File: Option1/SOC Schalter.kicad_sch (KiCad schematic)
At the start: 2 parts, among them Q1101 AON6284

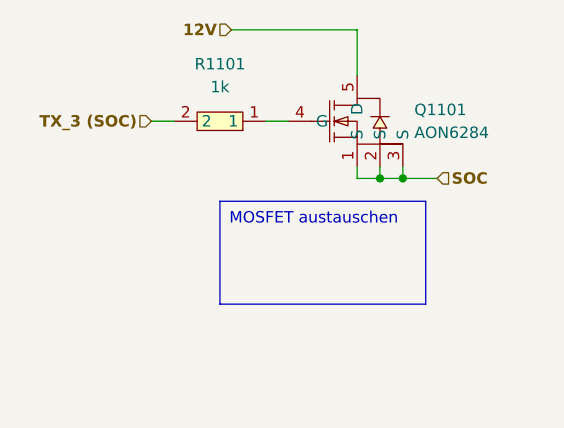
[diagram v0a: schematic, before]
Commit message: SPI Flash hinzugefügt, IN/Outputs vereinheitlicht, USB Flash Möglichkeit hinzugefügt, Display fehtl noch
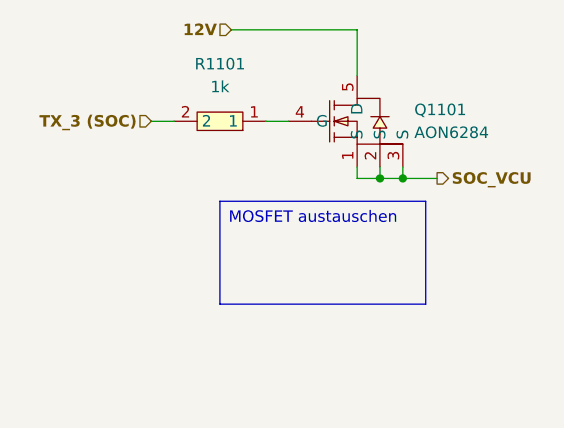
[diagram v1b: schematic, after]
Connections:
- net SOC renamed SOC_VCU
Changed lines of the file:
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@@
 (kicad_sch
-	(version 20231120)
+	(version 20250114)
 	(generator "eeschema")
-	(generator_version "8.0")
+	(generator_version "9.0")
 	(paper "A4")
 	(title_block
@@
 		(comment 2 "Bachelorarbiet")
 		(comment 3 "Sebastian Hampl")
+	)
+	(text_box "MOSFET austauschen"
+		(exclude_from_sim no)
+		(at 123.19 91.44 0)
+		(size 22.86 11.43)
+		(margins 0.9525 0.9525 0.9525 0.9525)
+		(stroke
+			(width 0)
+			(type default)
+			(color 255 0 0 1)
+		)
+		(fill
+			(type none)
+		)
+		(effects
+			(font
+				(size 1.27 1.27)
+			)
+			(justify left top)
+		)
 	)
 	(junction
@@
 		)
 	)
-	(text_box "MOSFET austauschen"
-		(exclude_from_sim no)
-		(at 123.19 91.44 0)
-		(size 22.86 11.43)
-		(stroke
-			(width 0)
-			(type default)
-			(color 255 0 0 1)
-		)
-		(fill
-			(type none)
-		)
-		(effects
-			(font
-				(size 1.27 1.27)
-			)
-			(justify left top)
-		)
-	)
-	(hierarchical_label "SOC"
-		(shape input)
+	(hierarchical_label "SOC_VCU"
+		(shape output)
 		(at 147.32 88.9 0)
 		(effects

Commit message: USB auf 3V3 umgebaut
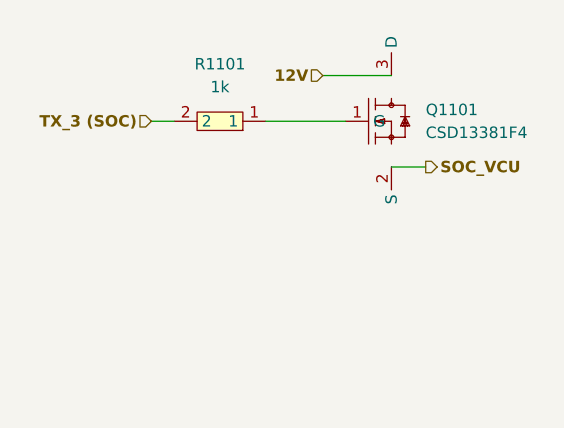
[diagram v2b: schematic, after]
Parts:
- removed Q1101: AON6284, easyeda2kicad:POWERVDFN-8_L6.2-W5.2-P1.27-LS6.0-BL, symbol easyeda2kicad:AON6284
- added Q1101: CSD13381F4, easyeda2kicad:PICOSTAR-3_L1.0-W0.6-P0.40-S0.65-BL-1, symbol EasyEda2KiCad:CSD13381F4
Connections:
- net 12V: now also Q1101.3 (D)
- net SOC_VCU: now also Q1101.2 (S)
- net at R1101.1: now also Q1101.1 (G)
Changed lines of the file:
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@@
 		(comment 3 "Sebastian Hampl")
-	)
-	(text_box "MOSFET austauschen"
-		(exclude_from_sim no)
-		(at 123.19 91.44 0)
-		(size 22.86 11.43)
-		(margins 0.9525 0.9525 0.9525 0.9525)
-		(stroke
-			(width 0)
-			(type default)
-			(color 255 0 0 1)
-		)
-		(fill
-			(type none)
-		)
-		(effects
-			(font
-				(size 1.27 1.27)
-			)
-			(justify left top)
-		)
-	)
-	(junction
-		(at 140.97 88.9)
-		(diameter 0)
-		(color 0 0 0 0)
-	)
-	(junction
-		(at 143.51 88.9)
-		(diameter 0)
-		(color 0 0 0 0)
-	)
-	(wire
-		(pts
-			(xy 140.97 88.9) (xy 138.43 88.9)
-		)
-		(stroke
-			(width 0)
-			(type default)
-		)
 	)
 	(wire
@@
 	(wire
 		(pts
-			(xy 143.51 88.9) (xy 140.97 88.9)
+			(xy 142.24 87.63) (xy 146.05 87.63)
 		)
 		(stroke
@@
 	(wire
 		(pts
-			(xy 138.43 88.9) (xy 138.43 87.63)
+			(xy 128.27 82.55) (xy 137.16 82.55)
 		)
 		(stroke
@@
 	(wire
 		(pts
-			(xy 128.27 82.55) (xy 130.81 82.55)
-		)
-		(stroke
-			(width 0)
-			(type default)
-		)
-	)
-	(wire
-		(pts
-			(xy 140.97 87.63) (xy 140.97 88.9)
-		)
-		(stroke
-			(width 0)
-			(type default)
-		)
-	)
-	(wire
-		(pts
-			(xy 124.46 72.39) (xy 138.43 72.39)
-		)
-		(stroke
-			(width 0)
-			(type default)
-		)
-	)
-	(wire
-		(pts
-			(xy 143.51 87.63) (xy 143.51 88.9)
-		)
-		(stroke
-			(width 0)
-			(type default)
-		)
-	)
-	(wire
-		(pts
-			(xy 143.51 88.9) (xy 147.32 88.9)
-		)
-		(stroke
-			(width 0)
-			(type default)
-		)
-	)
-	(wire
-		(pts
-			(xy 138.43 72.39) (xy 138.43 77.47)
+			(xy 134.62 77.47) (xy 142.24 77.47)
 		)
 		(stroke
@@
 	(hierarchical_label "SOC_VCU"
 		(shape output)
-		(at 147.32 88.9 0)
+		(at 146.05 87.63 0)
 		(effects
 			(font
@@
 	(hierarchical_label "12V"
 		(shape input)
-		(at 124.46 72.39 180)
+		(at 134.62 77.47 180)
 		(effects
 			(font
@@
 	)
 	(symbol
-		(lib_id "easyeda2kicad:AON6284")
-		(at 138.43 82.55 0)
+		(lib_id "EasyEda2KiCad:CSD13381F4")
+		(at 139.7 82.55 0)
 		(unit 1)
 		(exclude_from_sim no)
@@
 		(fields_autoplaced yes)
 		(property "Reference" "Q1101"
-			(at 144.78 81.2799 0)
+			(at 146.05 81.2799 0)
 			(effects
 				(font
@@
 			)
 		)
-		(property "Value" "AON6284"
-			(at 144.78 83.8199 0)
+		(property "Value" "CSD13381F4"
+			(at 146.05 83.8199 0)
 			(effects
 				(font
@@
 			)
 		)
-		(property "Footprint" "easyeda2kicad:POWERVDFN-8_L6.2-W5.2-P1.27-LS6.0-BL"
-			(at 138.43 95.25 0)
+		(property "Footprint" "easyeda2kicad:PICOSTAR-3_L1.0-W0.6-P0.40-S0.65-BL-1"
+			(at 139.7 95.25 0)
 			(effects
 				(font
@@
 		)
 		(property "Datasheet" ""
-			(at 138.43 82.55 0)
+			(at 139.7 82.55 0)
 			(effects
 				(font
@@
 		)
 		(property "Description" ""
-			(at 138.43 82.55 0)
+			(at 139.7 82.55 0)
 			(effects
 				(font
@@
 			)
 		)
-		(property "LCSC Part" "C3277770"
-			(at 138.43 97.79 0)
+		(property "LCSC Part" "C179868"
+			(at 139.7 97.79 0)
 			(effects
 				(font
@@
 			)
 		)
-		(pin "4"
-		)
-		(pin "2"
-		)
 		(pin "1"
 		)
 		(pin "3"
 		)
-		(pin "5"
+		(pin "2"
 		)
 		(instances
-			(project "Option1"
+			(project ""
 				(path "/b9e5f262-9648-4b79-bdd1-af888b822329/64070278-5fdb-4e21-a539-ae43b75eeb2e"
 					(reference "Q1101")

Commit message: Transitor getauscht, Pulldown Widerstände für Definierten LOW Pegel hinzugefügt
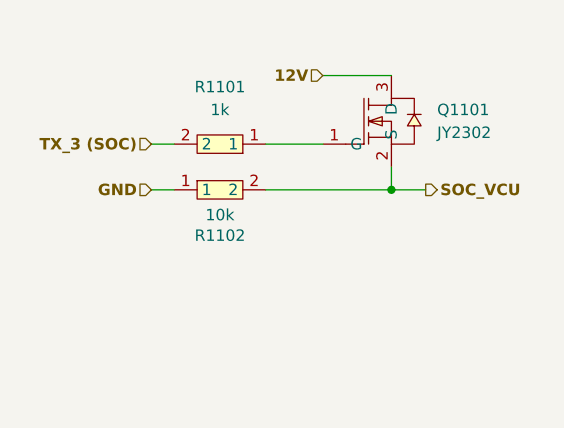
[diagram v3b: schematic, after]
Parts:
- removed Q1101: CSD13381F4, easyeda2kicad:PICOSTAR-3_L1.0-W0.6-P0.40-S0.65-BL-1, symbol EasyEda2KiCad:CSD13381F4
- added Q1101: JY2302, easyeda2kicad:SOT-23-3_L2.9-W1.3-P0.95-LS2.4-BR, symbol EasyEda2KiCad:JY2302
- added R1102: 10k, easyeda2kicad:R0603, symbol EasyEda2KiCad:0603WAF1002T5E
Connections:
- net 12V: now also Q1101.3 (D)
- net SOC_VCU: now also Q1101.2 (S), R1102.2
- net at R1101.1: now also Q1101.1 (G)
- new net GND: R1102.1
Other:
- moved on the sheet: R1101
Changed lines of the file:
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@@
 		(comment 3 "Sebastian Hampl")
 	)
-	(wire
-		(pts
-			(xy 115.57 82.55) (xy 118.11 82.55)
-		)
-		(stroke
-			(width 0)
-			(type default)
-		)
-	)
-	(wire
-		(pts
-			(xy 142.24 87.63) (xy 146.05 87.63)
-		)
-		(stroke
-			(width 0)
-			(type default)
-		)
-	)
-	(wire
-		(pts
-			(xy 128.27 82.55) (xy 137.16 82.55)
+	(junction
+		(at 142.24 90.17)
+		(diameter 0)
+		(color 0 0 0 0)
+	)
+	(wire
+		(pts
+			(xy 115.57 90.17) (xy 118.11 90.17)
+		)
+		(stroke
+			(width 0)
+			(type default)
+		)
+	)
+	(wire
+		(pts
+			(xy 115.57 85.09) (xy 118.11 85.09)
+		)
+		(stroke
+			(width 0)
+			(type default)
+		)
+	)
+	(wire
+		(pts
+			(xy 128.27 90.17) (xy 142.24 90.17)
+		)
+		(stroke
+			(width 0)
+			(type default)
+		)
+	)
+	(wire
+		(pts
+			(xy 142.24 90.17) (xy 142.24 87.63)
+		)
+		(stroke
+			(width 0)
+			(type default)
+		)
+	)
+	(wire
+		(pts
+			(xy 128.27 85.09) (xy 134.62 85.09)
 		)
 		(stroke
@@
 		(pts
 			(xy 134.62 77.47) (xy 142.24 77.47)
+		)
+		(stroke
+			(width 0)
+			(type default)
+		)
+	)
+	(wire
+		(pts
+			(xy 142.24 90.17) (xy 146.05 90.17)
 		)
 		(stroke
@@
 	(hierarchical_label "SOC_VCU"
 		(shape output)
-		(at 146.05 87.63 0)
+		(at 146.05 90.17 0)
 		(effects
 			(font
@@
 	(hierarchical_label "TX_3 (SOC)"
 		(shape input)
-		(at 115.57 82.55 180)
+		(at 115.57 85.09 180)
 		(effects
 			(font
@@
 		)
 	)
+	(hierarchical_label "GND"
+		(shape input)
+		(at 115.57 90.17 180)
+		(effects
+			(font
+				(size 1.27 1.27)
+				(thickness 0.254)
+				(bold yes)
+			)
+			(justify right)
+		)
+	)
 	(symbol
-		(lib_id "EasyEda2KiCad:CSD13381F4")
+		(lib_id "EasyEda2KiCad:JY2302")
 		(at 139.7 82.55 0)
 		(unit 1)
@@
 		(fields_autoplaced yes)
 		(property "Reference" "Q1101"
-			(at 146.05 81.2799 0)
+			(at 147.32 81.2799 0)
 			(effects
 				(font
@@
 			)
 		)
-		(property "Value" "CSD13381F4"
-			(at 146.05 83.8199 0)
+		(property "Value" "JY2302"
+			(at 147.32 83.8199 0)
 			(effects
 				(font
@@
 			)
 		)
-		(property "Footprint" "easyeda2kicad:PICOSTAR-3_L1.0-W0.6-P0.40-S0.65-BL-1"
+		(property "Footprint" "easyeda2kicad:SOT-23-3_L2.9-W1.3-P0.95-LS2.4-BR"
 			(at 139.7 95.25 0)
 			(effects
@@
 			)
 		)
-		(property "LCSC Part" "C179868"
+		(property "LCSC Part" "C3038095"
 			(at 139.7 97.79 0)
 			(effects
@@
 			)
 		)
+		(pin "3"
+		)
 		(pin "1"
 		)
-		(pin "3"
+		(pin "2"
+		)
+		(instances
+			(project "Option1"
+				(path "/b9e5f262-9648-4b79-bdd1-af888b822329/64070278-5fdb-4e21-a539-ae43b75eeb2e"
+					(reference "Q1101")
+					(unit 1)
+				)
+			)
+		)
+	)
+	(symbol
+		(lib_id "EasyEda2KiCad:0603WAF1002T5E")
+		(at 123.19 90.17 0)
+		(unit 1)
+		(exclude_from_sim no)
+		(in_bom yes)
+		(on_board yes)
+		(dnp no)
+		(property "Reference" "R1102"
+			(at 123.19 95.25 0)
+			(effects
+				(font
+					(size 1.27 1.27)
+				)
+			)
+		)
+		(property "Value" "10k"
+			(at 123.19 92.964 0)
+			(effects
+				(font
+					(size 1.27 1.27)
+				)
+			)
+		)
+		(property "Footprint" "easyeda2kicad:R0603"
+			(at 123.19 97.79 0)
+			(effects
+				(font
+					(size 1.27 1.27)
+				)
+				(hide yes)
+			)
+		)
+		(property "Datasheet" "https://lcsc.com/product-detail/Chip-Resistor-Surface-Mount-UniOhm_10KR-1002-1_C25804.html"
+			(at 123.19 100.33 0)
+			(effects
+				(font
+					(size 1.27 1.27)
+				)
+				(hide yes)
+			)
+		)
+		(property "Description" ""
+			(at 123.19 90.17 0)
+			(effects
+				(font
+					(size 1.27 1.27)
+				)
+				(hide yes)
+			)
+		)
+		(property "LCSC Part" "C25804"
+			(at 123.19 102.87 0)
+			(effects
+				(font
+					(size 1.27 1.27)
+				)
+				(hide yes)
+			)
+		)
+		(pin "1"
 		)
 		(pin "2"
@@
 			(project ""
 				(path "/b9e5f262-9648-4b79-bdd1-af888b822329/64070278-5fdb-4e21-a539-ae43b75eeb2e"
-					(reference "Q1101")
+					(reference "R1102")
 					(unit 1)
 				)
@@
 	(symbol
 		(lib_id "easyeda2kicad:0603WAF1001T5E")
-		(at 123.19 82.55 180)
+		(at 123.19 85.09 180)
 		(unit 1)
 		(exclude_from_sim no)
@@
 		(fields_autoplaced yes)
 		(property "Reference" "R1101"
-			(at 123.19 76.2 0)
+			(at 123.19 78.74 0)
 			(effects
 				(font
@@
 		)
 		(property "Value" "1k"
-			(at 123.19 78.74 0)
+			(at 123.19 81.28 0)
 			(effects
 				(font
@@
 		)
 		(property "Footprint" "easyeda2kicad:R0603"
+			(at 123.19 77.47 0)
+			(effects
+				(font
+					(size 1.27 1.27)
+				)
+				(hide yes)
+			)
+		)
+		(property "Datasheet" "https://lcsc.com/product-detail/Chip-Resistor-Surface-Mount-UniOhm_1KR-1001-1_C21190.html"
 			(at 123.19 74.93 0)
 			(effects
@@
 			)
 		)
-		(property "Datasheet" "https://lcsc.com/product-detail/Chip-Resistor-Surface-Mount-UniOhm_1KR-1001-1_C21190.html"
+		(property "Description" ""
+			(at 123.19 85.09 0)
+			(effects
+				(font
+					(size 1.27 1.27)
+				)
+				(hide yes)
+			)
+		)
+		(property "LCSC Part" "C21190"
 			(at 123.19 72.39 0)
 			(effects
 				(font
-					(size 1.27 1.27)
-				)
-				(hide yes)
-			)
-		)
-		(property "Description" ""
-			(at 123.19 82.55 0)
-			(effects
-				(font
-					(size 1.27 1.27)
-				)
-				(hide yes)
-			)
-		)
-		(property "LCSC Part" "C21190"
-			(at 123.19 69.85 0)
-			(effects
-				(font

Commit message: LEDs an Transistoren hinzugefügt, Layout angepasst, LEDs eingefügt, LEDs zeigen an, ob Transsitor durchgeschalten ist
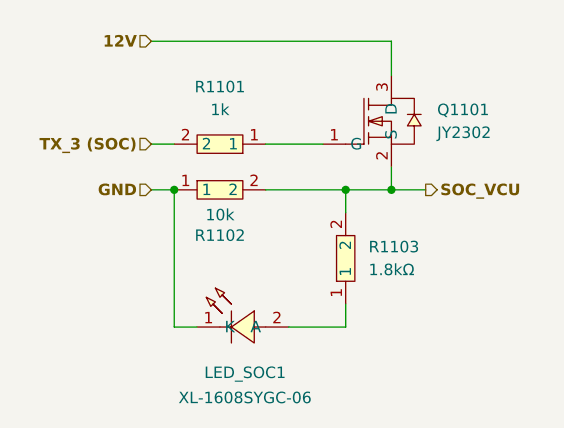
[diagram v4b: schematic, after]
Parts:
- added LED_SOC1: XL-1608SYGC-06, easyeda2kicad:LED0603-RD_GREEN, symbol EasyEda2KiCad:XL-1608SYGC-06
- added R1103: 1.8kΩ, easyeda2kicad:R0603, symbol EasyEda2KiCad:0603WAF1801T5E
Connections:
- net GND: now also LED_SOC1.1 (K)
- net SOC_VCU: now also R1103.2
- new net: LED_SOC1.2 (A), R1103.1
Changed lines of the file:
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@@
+	)
+	(junction
+		(at 137.16 90.17)
+		(diameter 0)
+		(color 0 0 0 0)
+	)
+	(junction
+		(at 118.11 90.17)
+		(diameter 0)
+		(color 0 0 0 0)
 	)
 	(junction
@@
 	(wire
 		(pts
+			(xy 137.16 90.17) (xy 137.16 92.71)
+		)
+		(stroke
+			(width 0)
+			(type default)
+		)
+	)
+	(wire
+		(pts
 			(xy 115.57 90.17) (xy 118.11 90.17)
 		)
@@
 	(wire
 		(pts
-			(xy 128.27 90.17) (xy 142.24 90.17)
+			(xy 137.16 90.17) (xy 142.24 90.17)
+		)
+		(stroke
+			(width 0)
+			(type default)
+		)
+	)
+	(wire
+		(pts
+			(xy 128.27 90.17) (xy 137.16 90.17)
+		)
+		(stroke
+			(width 0)
+			(type default)
+		)
+	)
+	(wire
+		(pts
+			(xy 118.11 105.41) (xy 118.11 90.17)
 		)
 		(stroke
@@
 	(wire
 		(pts
-			(xy 134.62 77.47) (xy 142.24 77.47)
+			(xy 137.16 102.87) (xy 137.16 105.41)
+		)
+		(stroke
+			(width 0)
+			(type default)
+		)
+	)
+	(wire
+		(pts
+			(xy 115.57 73.66) (xy 142.24 73.66)
+		)
+		(stroke
+			(width 0)
+			(type default)
+		)
+	)
+	(wire
+		(pts
+			(xy 142.24 73.66) (xy 142.24 77.47)
+		)
+		(stroke
+			(width 0)
+			(type default)
+		)
+	)
+	(wire
+		(pts
+			(xy 120.65 105.41) (xy 118.11 105.41)
+		)
+		(stroke
+			(width 0)
+			(type default)
+		)
+	)
+	(wire
+		(pts
+			(xy 130.81 105.41) (xy 137.16 105.41)
 		)
 		(stroke
@@
 	(hierarchical_label "12V"
 		(shape input)
-		(at 134.62 77.47 180)
+		(at 115.57 73.66 180)
 		(effects
 			(font
@@
 		)
 	)
+	(symbol
+		(lib_id "EasyEda2KiCad:XL-1608SYGC-06")
+		(at 125.73 105.41 0)
+		(unit 1)
+		(exclude_from_sim no)
+		(in_bom yes)
+		(on_board yes)
+		(dnp no)
+		(property "Reference" "LED_SOC1"
+			(at 125.984 110.49 0)
+			(effects
+				(font
+					(size 1.27 1.27)
+				)
+			)
+		)
+		(property "Value" "XL-1608SYGC-06"
+			(at 125.984 113.284 0)
+			(effects
+				(font
+					(size 1.27 1.27)
+				)
+			)
+		)
+		(property "Footprint" "easyeda2kicad:LED0603-RD_GREEN"
+			(at 125.73 113.03 0)
+			(effects
+				(font
+					(size 1.27 1.27)
+				)
+				(hide yes)
+			)
+		)
+		(property "Datasheet" ""
+			(at 125.73 105.41 0)
+			(effects
+				(font
+					(size 1.27 1.27)
+				)
+				(hide yes)
+			)
+		)
+		(property "Description" ""
+			(at 125.73 105.41 0)
+			(effects
+				(font
+					(size 1.27 1.27)
+				)
+				(hide yes)
+			)
+		)
+		(property "LCSC Part" "C965805"
+			(at 125.73 115.57 0)
+			(effects
+				(font
+					(size 1.27 1.27)
+				)
+				(hide yes)
+			)
+		)
+		(pin "2"
+		)
+		(pin "1"
+		)
+		(instances
+			(project "Option1"
+				(path "/b9e5f262-9648-4b79-bdd1-af888b822329/64070278-5fdb-4e21-a539-ae43b75eeb2e"
+					(reference "LED_SOC1")
+					(unit 1)
+				)
+			)
+		)
+	)
+	(symbol
+		(lib_id "EasyEda2KiCad:0603WAF1801T5E")
+		(at 137.16 97.79 90)
+		(unit 1)
+		(exclude_from_sim no)
+		(in_bom yes)
+		(on_board yes)
+		(dnp no)
+		(fields_autoplaced yes)
+		(property "Reference" "R1103"
+			(at 139.7 96.5199 90)
+			(effects
+				(font
+					(size 1.27 1.27)
+				)
+				(justify right)
+			)
+		)
+		(property "Value" "1.8kΩ"
+			(at 139.7 99.0599 90)
+			(effects
+				(font
+					(size 1.27 1.27)
+				)
+				(justify right)
+			)
+		)
+		(property "Footprint" "easyeda2kicad:R0603"
+			(at 144.78 97.79 0)
+			(effects
+				(font
+					(size 1.27 1.27)
+				)
+				(hide yes)
+			)
+		)
+		(property "Datasheet" "https://lcsc.com/product-detail/Chip-Resistor-Surface-Mount-UniOhm_1-8KR-1801-1_C4177.html"
+			(at 147.32 97.79 0)
+			(effects
+				(font
+					(size 1.27 1.27)
+				)
+				(hide yes)
+			)
+		)
+		(property "Description" ""
+			(at 137.16 97.79 0)
+			(effects
+				(font
+					(size 1.27 1.27)
+				)
+				(hide yes)
+			)
+		)
+		(property "LCSC Part" "C4177"
+			(at 149.86 97.79 0)
+			(effects
+				(font
+					(size 1.27 1.27)
+				)
+				(hide yes)
+			)
+		)
+		(pin "1"
+		)
+		(pin "2"
+		)
+		(instances
+			(project "Option1"
+				(path "/b9e5f262-9648-4b79-bdd1-af888b822329/64070278-5fdb-4e21-a539-ae43b75eeb2e"
+					(reference "R1103")
+					(unit 1)
+				)
+			)
+		)
+	)
